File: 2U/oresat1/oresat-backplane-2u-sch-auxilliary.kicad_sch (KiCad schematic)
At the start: 2 parts

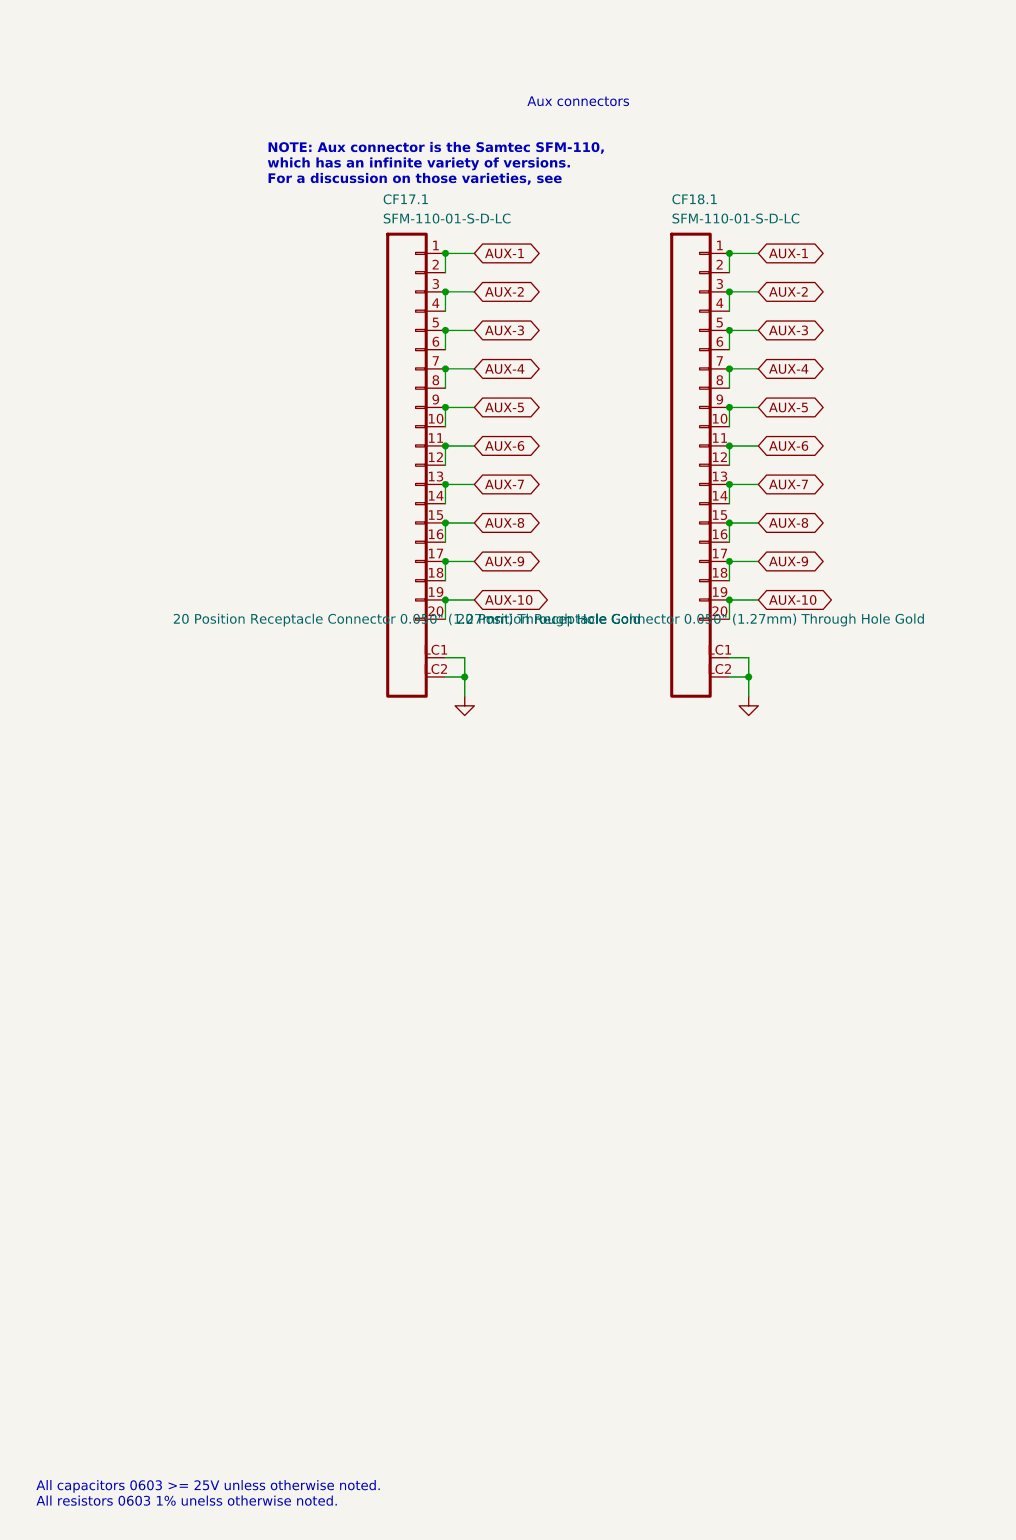
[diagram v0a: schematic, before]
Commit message: Update of OreSat1 2U backplane. Removed extraneous connectors, imported DXF from OnShape and moved debug connectors by 0.176 mm. Routing left to do.
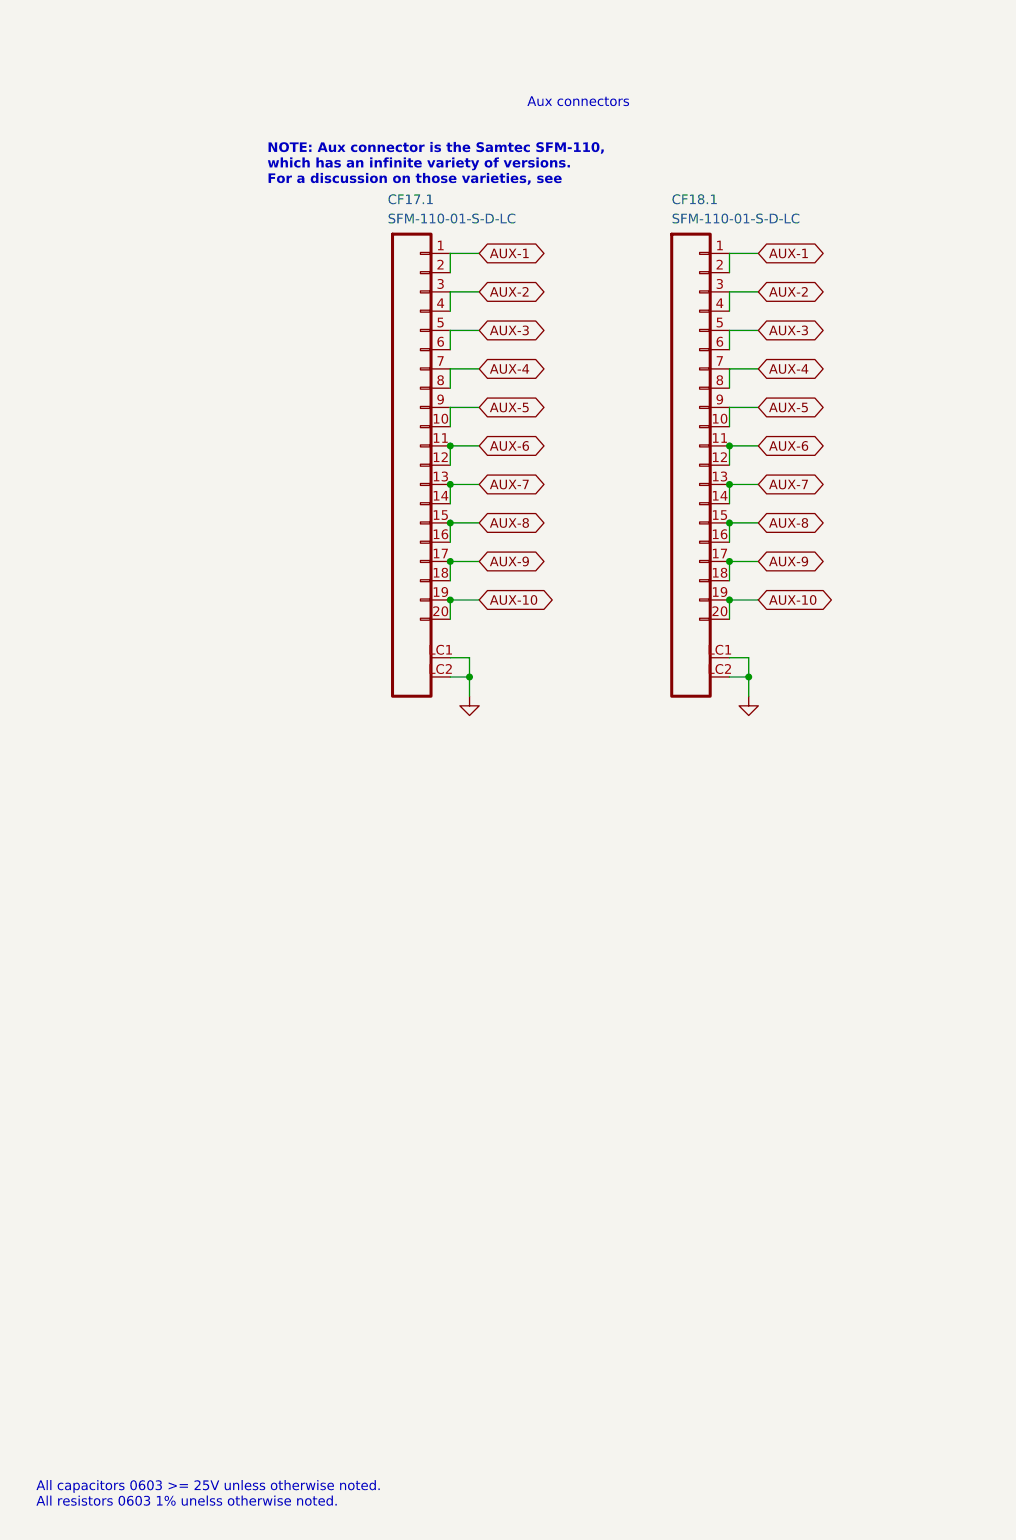
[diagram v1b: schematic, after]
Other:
- moved on the sheet: CF17.1

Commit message: Fix library issues on aux footprints.
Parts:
- CF17.1, CF18.1: symbol oresat-connectors:J-SAMTEC-TFM-110-01-L-D-RA -> oresat-connectors:J-SAMTEC-SFM-110-X1-XXX-D-LC
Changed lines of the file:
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@@
 	)
 	(symbol
-		(lib_name "J-SAMTEC-TFM-110-01-L-D-RA_1")
-		(lib_id "oresat-connectors:J-SAMTEC-TFM-110-01-L-D-RA")
+		(lib_id "oresat-connectors:J-SAMTEC-SFM-110-X1-XXX-D-LC")
 		(at 166.37 147.32 0)
 		(unit 1)
@@
 		)
 		(property "Footprint" "oresat-connectors:J-SAMTEC-CF-SFM-110-X1-XXX-D-LC"
-			(at 166.37 147.32 0)
+			(at 171.45 207.01 0)
 			(effects
 				(font
@@
 		)
 		(property "Datasheet" "https://suddendocs.samtec.com/catalog_english/sfm.pdf"
-			(at 166.37 147.32 0)
+			(at 168.91 210.82 0)
 			(effects
 				(font
@@
 			)
 		)
-		(property "Description" "20 Position Receptacle Connector 0.050\" (1.27mm) Through Hole Gold"
+		(property "Description" "OreSat backplane connector, 2x20 RA"
 			(at 166.37 147.32 0)
 			(effects
@@
 	)
 	(symbol
-		(lib_id "oresat-connectors:J-SAMTEC-TFM-110-01-L-D-RA")
+		(lib_id "oresat-connectors:J-SAMTEC-SFM-110-X1-XXX-D-LC")
 		(at 203.2 147.32 0)
 		(unit 1)
@@
 		)
 		(property "Footprint" "oresat-connectors:J-SAMTEC-CF-SFM-110-X1-XXX-D-LC"
-			(at 203.2 147.32 0)
+			(at 208.28 207.01 0)
 			(effects
 				(font
@@
 		)
 		(property "Datasheet" "https://suddendocs.samtec.com/catalog_english/sfm.pdf"
-			(at 203.2 147.32 0)
+			(at 205.74 210.82 0)
 			(effects
 				(font
@@
 			)
 		)
-		(property "Description" "20 Position Receptacle Connector 0.050\" (1.27mm) Through Hole Gold"
+		(property "Description" "OreSat backplane connector, 2x20 RA"
 			(at 203.2 147.32 0)
 			(effects

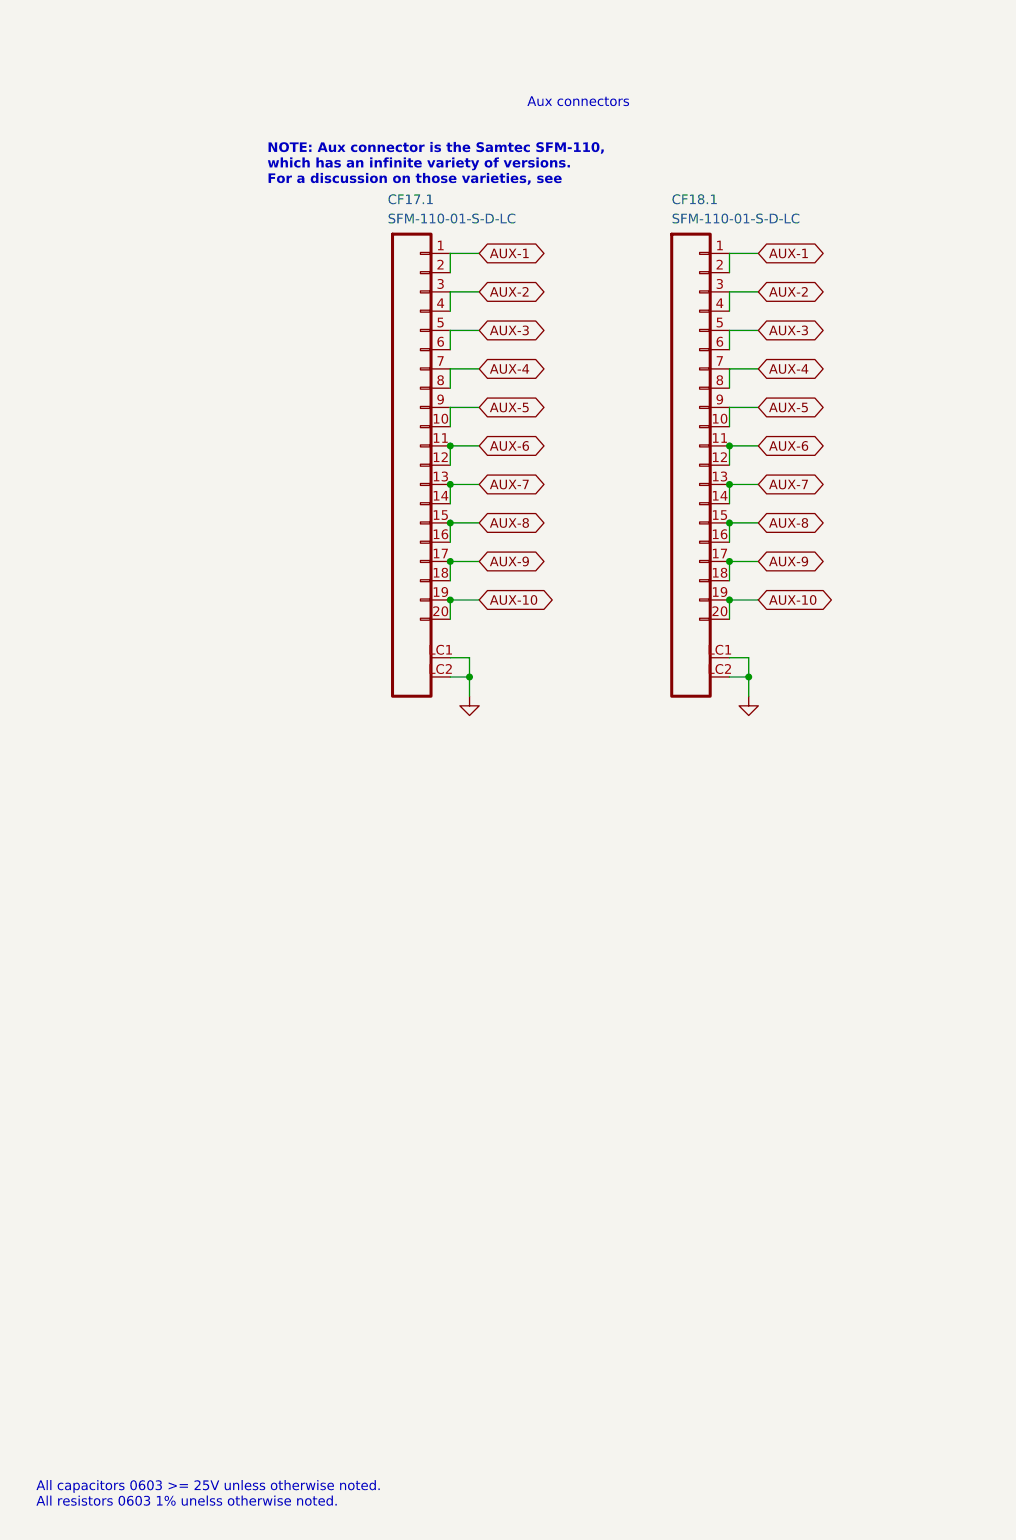
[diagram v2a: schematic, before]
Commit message: Final fix and polish on 2U backplane for OreSat1.
Found a bunch of small little details to fix - somehow CAN lines were down to 0.2 mm, fixed to 0.3 mm. Also expanded some of
the lines to 0.6 mm for higher power lines. Added more vias for VBUS on the debug connector, and finally added 3D models
to all of the connectors so the backplane fully renders now!
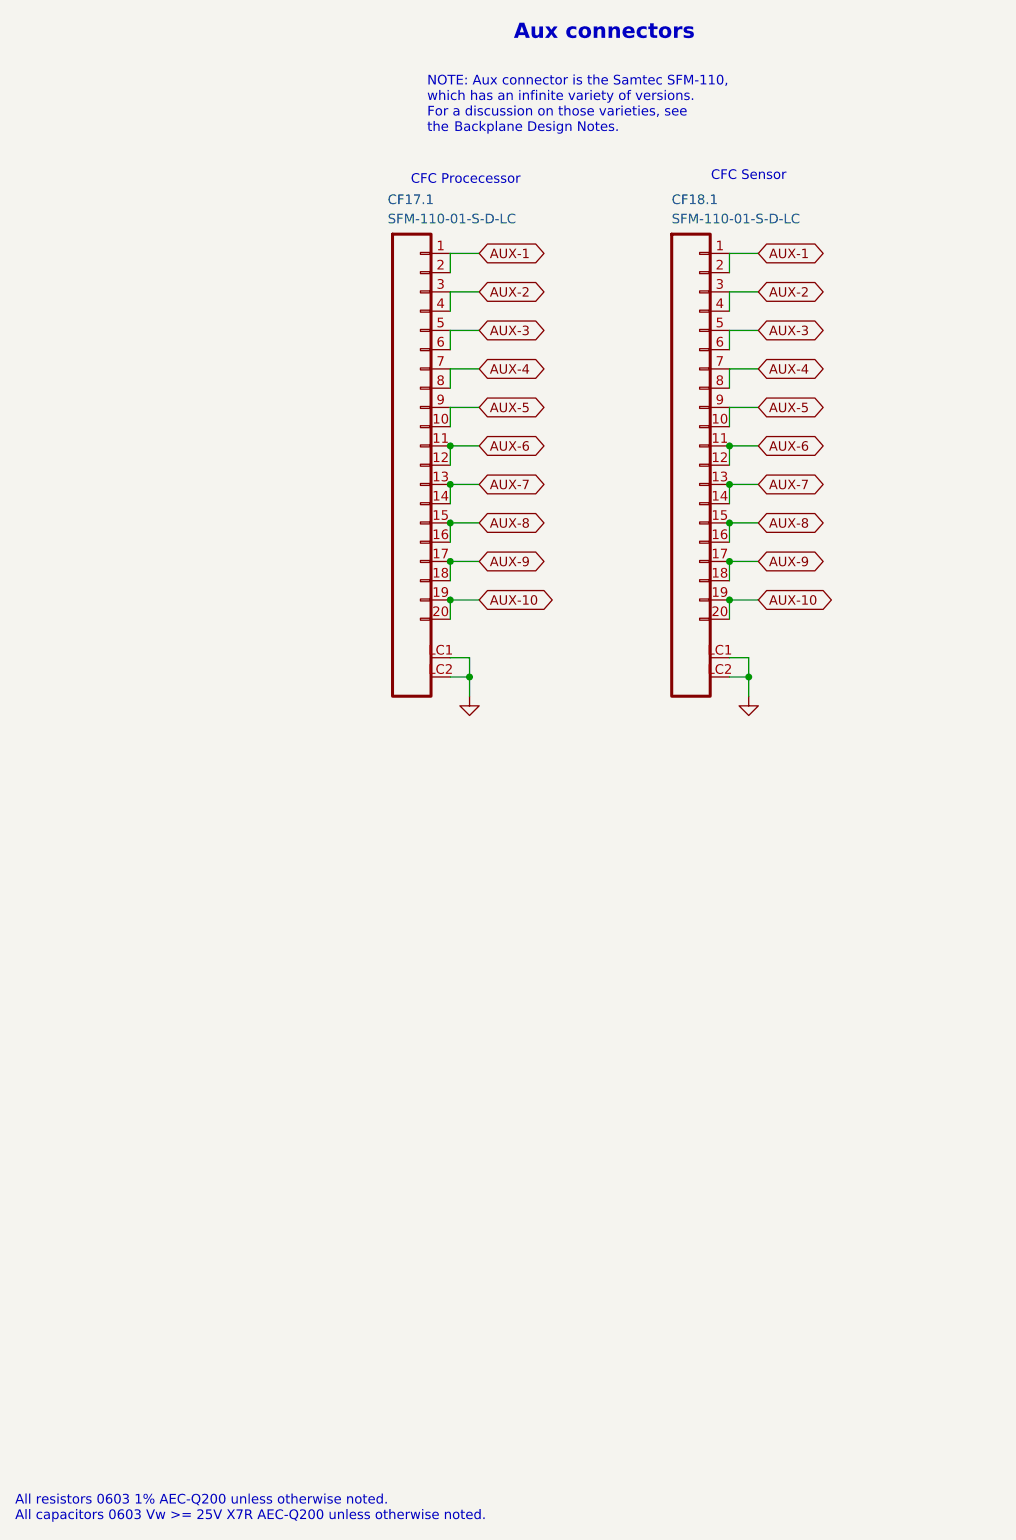
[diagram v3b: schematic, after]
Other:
- note added: "All resistors 0603 1% AEC-Q200 unless otherwise noted. All capacitors 0603 Vw >= 25V X7R AEC-Q200 unless otherwise noted."
- note added: "Backplane Design Notes."
- note added: "CFC Procecessor"
- note added: "CFC Sensor"
- note added: "NOTE: Aux connector is the Samtec SFM-110, which has an infinite variety of versions. For a discussion on those varieties, see the"
- note removed: "All capacitors 0603 >= 25V unless otherwise noted. All resistors 0603 1% unelss otherwise noted."
- note removed: "NOTE: Aux connector is the Samtec SFM-110, which has an infinite variety of versions. For a discussion on those varieties, see"
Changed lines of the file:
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@@
 	(title_block
 		(title "OreSat1 2U Backplane")
-		(date "2025-09-28")
+		(date "2025-11-30")
 		(rev "1.0")
 		(company "Portland State Aerospace Society")
 	)
-	(text "NOTE: Aux connector is the Samtec SFM-110, \nwhich has an infinite variety of versions.\nFor a discussion on those varieties, see"
+	(text "Backplane Design Notes."
 		(exclude_from_sim no)
-		(at 147.32 90.17 0)
+		(at 171.958 83.312 0)
 		(effects
 			(font
 				(size 1.27 1.27)
-				(thickness 0.254)
-				(bold yes)
+				(thickness 0.1588)
 			)
 			(justify left bottom)
+			(href "https://docs.google.com/document/d/1zO-TTvM27BjbEozDkhhjdMhfOL7Qgdrsm62HG446hcQ/edit?usp=sharing")
 		)
 	)
-	(text "Aux connectors"
+	(text "CFC Procecessor"
 		(exclude_from_sim no)
-		(at 181.61 80.01 0)
+		(at 173.482 89.408 0)
 		(effects
 			(font
 				(size 1.27 1.27)
 			)
-			(justify left bottom)
 		)
 	)
-	(text "All capacitors 0603 >= 25V unless otherwise noted.\nAll resistors 0603 1% unelss otherwise noted."
+	(text "All resistors 0603 1% AEC-Q200 unless otherwise noted.\nAll capacitors 0603 Vw >= 25V X7R AEC-Q200 unless otherwise noted.\n"
 		(exclude_from_sim no)
-		(at 116.84 262.89 0)
+		(at 114.046 264.668 0)
 		(effects
 			(font
@@
 		)
 	)
+	(text "CFC Sensor"
+		(exclude_from_sim no)
+		(at 210.82 88.9 0)
+		(effects
+			(font
+				(size 1.27 1.27)
+			)
+		)
+	)
+	(text "NOTE: Aux connector is the Samtec SFM-110, \nwhich has an infinite variety of versions.\nFor a discussion on those varieties, see \nthe"
+		(exclude_from_sim no)
+		(at 168.402 83.312 0)
+		(effects
+			(font
+				(size 1.27 1.27)
+				(thickness 0.1588)
+			)
+			(justify left bottom)
+		)
+	)
+	(text "Aux connectors"
+		(exclude_from_sim no)
+		(at 179.832 71.12 0)
+		(effects
+			(font
+				(size 2 2)
+				(thickness 0.4)
+				(bold yes)
+			)
+			(justify left bottom)
+		)
+	)
